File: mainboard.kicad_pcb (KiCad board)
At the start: 2 copper layers, 70 x 60 mm, 25 parts, among them J1 terminal_led-strip, J2 header_rotary-encoder, J3 AudioJack2, J4 header_rpi, J5 power_input, Q1 IRF9540N, SW1 power_switch, U1 ATtiny84A-P, U2 MSGEQ7, U3 OPA197xDBV, U4 logic-level-converter

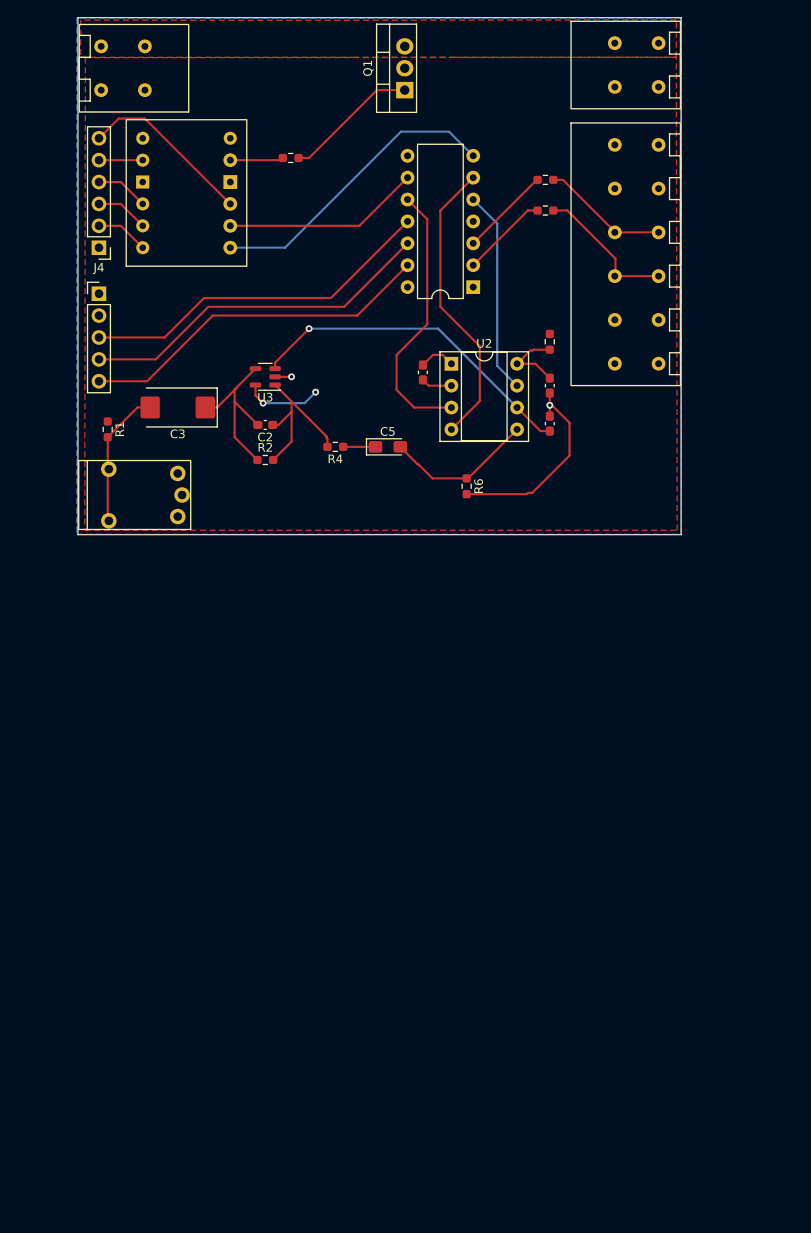
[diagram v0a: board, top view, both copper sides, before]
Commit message: start routing tracks
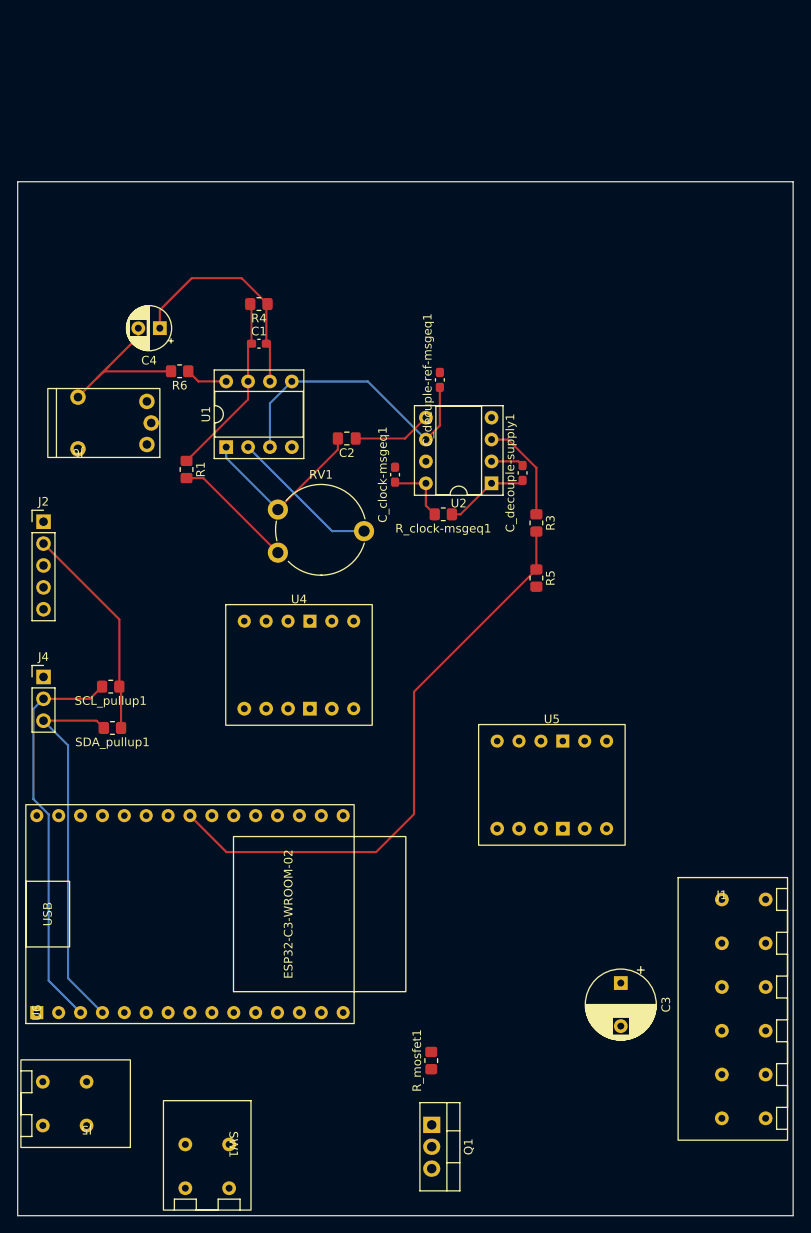
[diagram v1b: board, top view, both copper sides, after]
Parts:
- removed C5: 0.22u, Capacitor_Tantalum_SMD:CP_EIA-3216-18_Kemet-A_Pad1.58x1.35mm_HandSolder
- removed J3: AudioJack2, my_lib:jack_3.5mm_TS-only
- removed R2: 170k, Resistor_SMD:R_0603_1608Metric_Pad0.98x0.95mm_HandSolder
- removed R_led-strip_1, R_led-strip_2: 220, Resistor_SMD:R_0603_1608Metric_Pad0.98x0.95mm_HandSolder
- removed U3: OPA197xDBV, Package_TO_SOT_SMD:SOT-23-5
- added C1: 7p, Capacitor_SMD:C_0603_1608Metric_Pad1.08x0.95mm_HandSolder, F.Cu at (78.0, 68.8)
- added C4: 5.6u, Capacitor_THT:CP_Radial_D5.0mm_P2.50mm, F.Cu at (66.5, 67.0)
- added J6: AudioJack2, my_lib:jack_3.5mm_TS-only, F.Cu at (57.0, 81.0)
- added R3: 1M, Resistor_SMD:R_0805_2012Metric_Pad1.20x1.40mm_HandSolder, F.Cu at (110.2, 89.6)
- added R5: 2M, Resistor_SMD:R_0805_2012Metric_Pad1.20x1.40mm_HandSolder, F.Cu at (110.2, 96.0)
- added RV1: 5k, Potentiometer_THT:Potentiometer_Piher_PT-10-V10_Vertical, F.Cu at (80.2, 93.0)
- added SCL_pullup1: 2k, Resistor_SMD:R_0805_2012Metric_Pad1.20x1.40mm_HandSolder, F.Cu at (60.8, 108.6)
- added SDA_pullup1: 2k, Resistor_SMD:R_0805_2012Metric_Pad1.20x1.40mm_HandSolder, F.Cu at (61.0, 113.4)
- added U5: logic-level-converter, my_lib:sparkfun_logic_level_converter_bidirectional, F.Cu at (112.0, 120.0)
- added U6: ~, my_lib:esp32_c3_dev-kit-c_02, F.Cu at (52.2, 146.4)
- C2: value 7p -> C; footprint Capacitor_SMD:C_0603_1608Metric_Pad1.08x0.95mm_HandSolder -> Capacitor_SMD:C_0805_2012Metric_Pad1.18x1.45mm_HandSolder
- C3: value 5.6u -> C_Polarized; footprint Capacitor_Tantalum_SMD:CP_EIA-7343-31_Kemet-D_Pad2.25x2.55mm_HandSolder -> Capacitor_THT:CP_Radial_D8.0mm_P5.00mm
- J4: value header_rpi -> header_pi; footprint Connector_PinHeader_2.54mm:PinHeader_1x06_P2.54mm_Vertical -> Connector_PinHeader_2.54mm:PinHeader_1x03_P2.54mm_Vertical
- R1: value 6k -> 1k; footprint Resistor_SMD:R_0603_1608Metric_Pad0.98x0.95mm_HandSolder -> Resistor_SMD:R_0805_2012Metric_Pad1.20x1.40mm_HandSolder
- R4: value 50 -> 170k; footprint Resistor_SMD:R_0603_1608Metric_Pad0.98x0.95mm_HandSolder -> Resistor_SMD:R_0805_2012Metric_Pad1.20x1.40mm_HandSolder
- R6: value 100k -> 6k; footprint Resistor_SMD:R_0603_1608Metric_Pad0.98x0.95mm_HandSolder -> Resistor_SMD:R_0805_2012Metric_Pad1.20x1.40mm_HandSolder
- R_clock-msgeq1, R_mosfet1: footprint Resistor_SMD:R_0603_1608Metric_Pad0.98x0.95mm_HandSolder -> Resistor_SMD:R_0805_2012Metric_Pad1.20x1.40mm_HandSolder
- U1: value ATtiny84A-P -> OPA2277; footprint Package_DIP:DIP-14_W7.62mm -> Package_DIP:DIP-8_W7.62mm_Socket
- moved SW1 135.4 mm to (74.5, 161.7), turned to -90 degrees
- moved J5 120.4 mm to (58.0, 159.5)
- moved Q1 120.1 mm to (98.1, 159.5), turned to -90 degrees
- moved R_mosfet1 106.0 mm to (98.0, 152.0), turned to 90 degrees
- moved J1 88.5 mm to (131.7, 133.3)
- moved C3 84.3 mm to (120.0, 143.0), turned to -90 degrees
- moved U4 56.3 mm to (82.7, 106.1), turned to 0 degrees
- moved J4 50.2 mm to (53.0, 107.5), turned to 0 degrees
- moved R6 35.9 mm to (68.8, 72.0), turned to 180 degrees
- moved U1 34.2 mm to (74.2, 80.8), turned to 90 degrees
- moved J2 27.2 mm to (53.0, 89.5)
- moved R_clock-msgeq1 23.5 mm to (99.4, 88.6), turned to 180 degrees
- moved C_clock-msgeq1 20.7 mm to (93.8, 84.0), turned to 90 degrees
- moved R4 18.8 mm to (78.0, 64.2)
- moved C_decouple-supply1 16.4 mm to (108.6, 83.8), turned to 90 degrees
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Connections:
- C2 pad 1: Net-(C2-Pad1) -> msgeq7-in
- C2 pad 2: Net-(U3--) -> Net-(C2-Pad2)
- C3 pad 1: Net-(U3--) -> 5V_led
- C3 pad 2: Net-(C3-Pad2) -> GND
- C_decouple-supply1 pad 1: /power-on -> 5V
- C_decuple-ref-msgeq1 pad 1: Net-(U2-GND) -> V_ref
- J1 pad 1: /power-on -> GND
- J1 pad 2: /power-on -> Net-(J1-Pin_2)
- J1 pad 3: Net-(J1-Pin_3) -> 5V_led
- J1 pad 4: Net-(J1-Pin_4) -> GND
- J1 pad 5: GND -> Net-(J1-Pin_5)
- J1 pad 6: GND -> 5V_led
- J2 pad 2: /power-on -> 3V3
- J2 pad 3: Net-(J2-Pin_3) -> rotary_sw
- J2 pad 4: Net-(J2-Pin_4) -> rotary_dt
- J2 pad 5: Net-(J2-Pin_5) -> rotary_clk
- Q1 pad 2: /power-on -> 5V_led
- Q1 pad 3: +5V -> 5V
- R1 pad 1: /power-on -> preamp_out
- R1 pad 2: Net-(C3-Pad2) -> Net-(R1-Pad2)
- R4 pad 1: Net-(C5-Pad1) -> Net-(U1B--)
- R4 pad 2: Net-(C2-Pad1) -> preamp_out
- R6 pad 1: Net-(U2-IN) -> 5V
- R6 pad 2: GND -> Net-(C4-Pad2)
- R_clock-msgeq1 pad 1: /power-on -> 5V
- R_mosfet1 pad 1: Net-(U4-LV3) -> power_fet
- SW1 pad 1: +5V -> 5V
- SW1 pad 2: /power-on -> +5V
- U1 pad 1: /power-on -> Net-(C2-Pad2)
- U1 pad 3: Net-(U1-XTAL2/PB1) -> V_ref
- U1 pad 4: unconnected-(U1-~{RESET}/PB3-Pad4) -> GND
- U1 pad 5: Net-(U1-PB2) -> V_ref
- U1 pad 6: Net-(U1-PA7) -> Net-(U1B--)
- U1 pad 7: Net-(U1-PA6) -> preamp_out
- U1 pad 8: unconnected-(U1-PA5-Pad8) -> 5V
- U2 pad 1: /power-on -> 5V
- U2 pad 3: Net-(U1-PA3) -> msgeq7-out
- U2 pad 4: Net-(U1-PA7) -> msgeq7-strobe
- U2 pad 5: Net-(U2-IN) -> msgeq7-in
- U2 pad 6: Net-(U2-GND) -> V_ref
- U2 pad 7: Net-(U1-PB2) -> msgeq7-reset
- U4 pad 1: Net-(U1-PA6) -> esp_led-strip_front
- U4 pad 10: Net-(J4-Pin_4) -> 5V
- U4 pad 11: Net-(J4-Pin_3) -> Net-(J1-Pin_5)
- U4 pad 12: Net-(J4-Pin_2) -> Net-(J1-Pin_2)
- U4 pad 2: Net-(U1-PA4) -> esp_led-strip_back
- U4 pad 3: Net-(J4-Pin_6) -> 3V3
- U4 pad 5: Net-(U4-LV3) -> esp_msgeq7-strobe
- U4 pad 6: unconnected-(U4-LV4-Pad6) -> esp_msgeq7-reset
- U4 pad 7: unconnected-(U4-HV4-Pad7) -> msgeq7-reset
- U4 pad 8: Net-(J4-Pin_5) -> msgeq7-strobe
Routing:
- net Net-(U6-4): track 0.00 -> 68.3 mm
- net Net-(J2-Pin_5): track 41.4 -> 0.00 mm
- net Net-(J2-Pin_4): track 41.4 -> 0.00 mm
- net Net-(J2-Pin_3): track 41.4 -> 0.00 mm
- net Net-(J4-Pin_2): track 6.13 -> 46.6 mm
- net Net-(U2-GND): track 39.1 -> 0.00 mm, vias 1 -> 0
- net Net-(J4-Pin_3): track 6.13 -> 44.1 mm
- net Net-(U1-PA6): track 34.9 -> 0.00 mm
- net Net-(U1-PA7): track 34.1 -> 0.00 mm
- net V_ref: track 0.00 -> 33.8 mm
- net Net-(U1-PA3): track 31.7 -> 0.00 mm
- net Net-(U1B--): track 0.00 -> 26.6 mm
- net 3V3: track 0.00 -> 25.1 mm
- net GND: track 28.9 -> 3.80 mm, vias 2 -> 0
- net Net-(U1-PB2): track 23.7 -> 0.00 mm
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- removed copper zone on F.Cu, net +5V
- removed copper zone on F.Cu, net /power-on
- removed copper zone on B.Cu, net GND
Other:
- board size 70 x 60 mm -> 90 x 120 mm

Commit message: route tracks and add mounting holes
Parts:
- removed U6: ~, my_lib:esp32_c3_dev-kit-c_02
- added REF**: MountingHole_3.2mm_M3_DIN965_Pad, MountingHole:MountingHole_3.2mm_M3_DIN965_Pad, F.Cu at (125.0, 65.0)
- added REF**: MountingHole_3.2mm_M3_DIN965_Pad, MountingHole:MountingHole_3.2mm_M3_DIN965_Pad, F.Cu at (55.0, 165.0)
- added REF**: MountingHole_3.2mm_M3_DIN965_Pad, MountingHole:MountingHole_3.2mm_M3_DIN965_Pad, F.Cu at (125.0, 165.0)
- added REF**: MountingHole_3.2mm_M3_DIN965_Pad, MountingHole:MountingHole_3.2mm_M3_DIN965_Pad, F.Cu at (55.0, 65.0)
- added U3: ~, my_lib:esp32_c3_dev-kit-c_02, F.Cu at (52.2, 146.4)
- C1, C_clock-msgeq1, C_decouple-supply1, C_decuple-ref-msgeq1: footprint Capacitor_SMD:C_0603_1608Metric_Pad1.08x0.95mm_HandSolder -> Capacitor_SMD:C_0805_2012Metric_Pad1.18x1.45mm_HandSolder
- moved C3 16.0 mm to (108.4, 154.0)
- moved J1 10.2 mm to (121.5, 133.2)
- moved J5 2.54 mm to (58.0, 157.0)
- turned R_mosfet1 to -90 degrees
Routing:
- net 5V: track 15.0 -> 172.8 mm
- net rotary_sw: track 0.00 -> 89.4 mm, vias 0 -> 1
- net Net-(J1-Pin_5): track 0.00 -> 88.7 mm
- net rotary_dt: track 0.00 -> 87.9 mm, vias 0 -> 1
- net rotary_clk: track 0.00 -> 86.4 mm, vias 0 -> 1
- net 3V3: track 25.1 -> 102.1 mm
- net Net-(J1-Pin_2): track 0.00 -> 70.1 mm
- net Net-(U3-GPIO10): track 0.00 -> 49.7 mm
- net power_fet: track 0.00 -> 44.4 mm
- net msgeq7-strobe: track 0.00 -> 35.5 mm
- net esp_msgeq7-reset: track 0.00 -> 28.0 mm
- net esp_led-strip_back: track 0.00 -> 25.6 mm
- net msgeq7-reset: track 0.00 -> 22.0 mm
- net Net-(U3-GPIO4/ADC1_CH4): track 68.3 -> 51.4 mm
- net esp_led-strip_front: track 0.00 -> 16.1 mm
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- added copper zone on F.Cu, net +5V
- added copper zone on F.Cu, net 5V
- added copper zone on F.Cu, net 5V_led
- added copper zone on B.Cu, net GND
- added copper zone on F.Cu, net GND
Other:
- board size 90 x 120 mm -> 80 x 110 mm

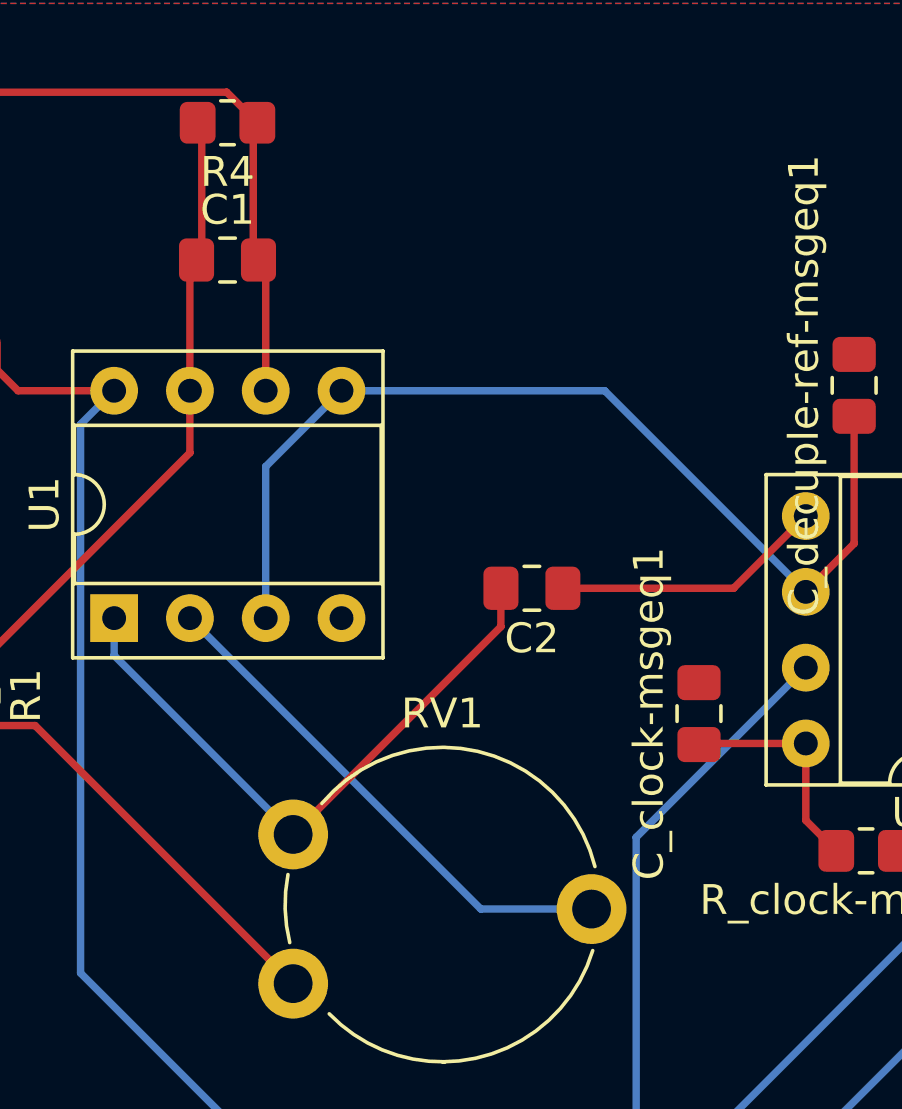
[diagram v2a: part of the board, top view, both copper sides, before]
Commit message: add jlc part ids
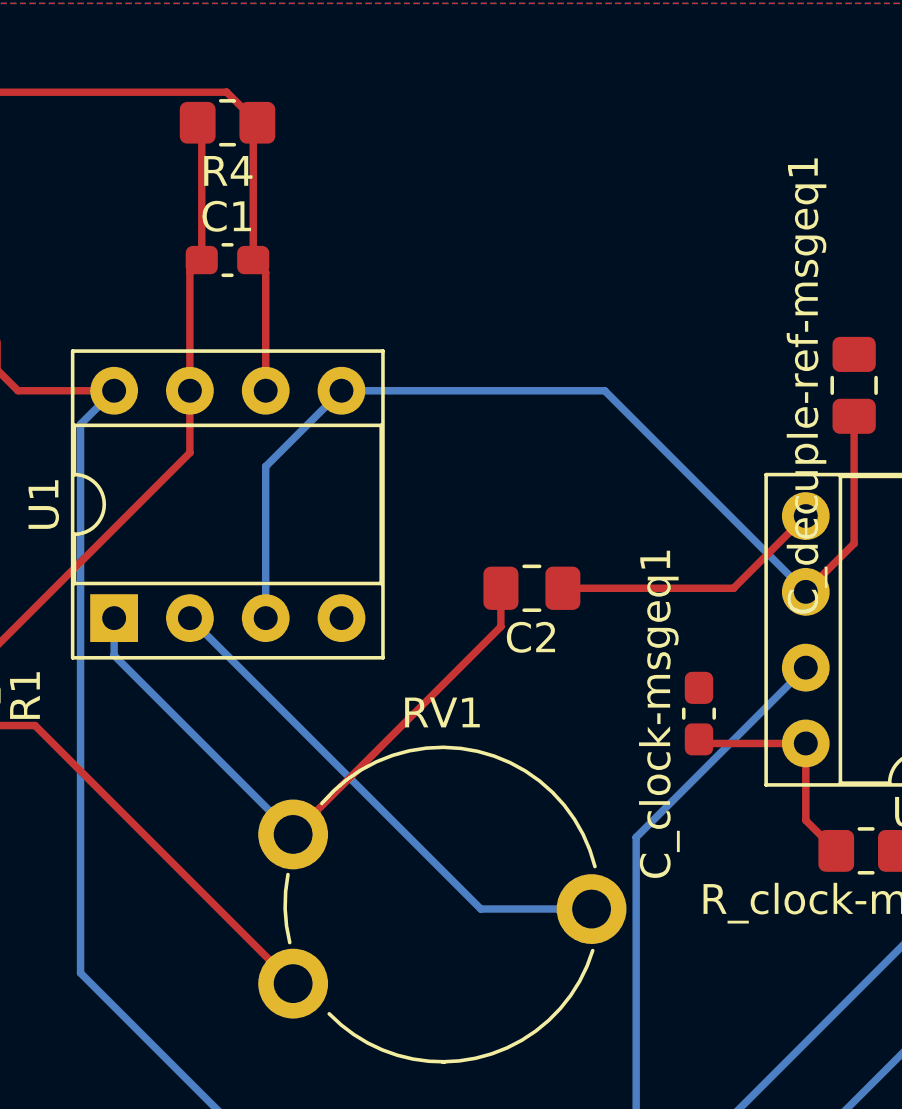
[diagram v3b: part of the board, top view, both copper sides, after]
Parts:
- C1: value 7p -> 10p; footprint Capacitor_SMD:C_0805_2012Metric_Pad1.18x1.45mm_HandSolder -> Capacitor_SMD:C_0603_1608Metric_Pad1.08x0.95mm_HandSolder
- C2: value C -> 220n
- C_clock-msgeq1: footprint Capacitor_SMD:C_0805_2012Metric_Pad1.18x1.45mm_HandSolder -> Capacitor_SMD:C_0603_1608Metric_Pad1.08x0.95mm_HandSolder
- R4: value 170k -> 150k
- R6: value 6k -> 5k6

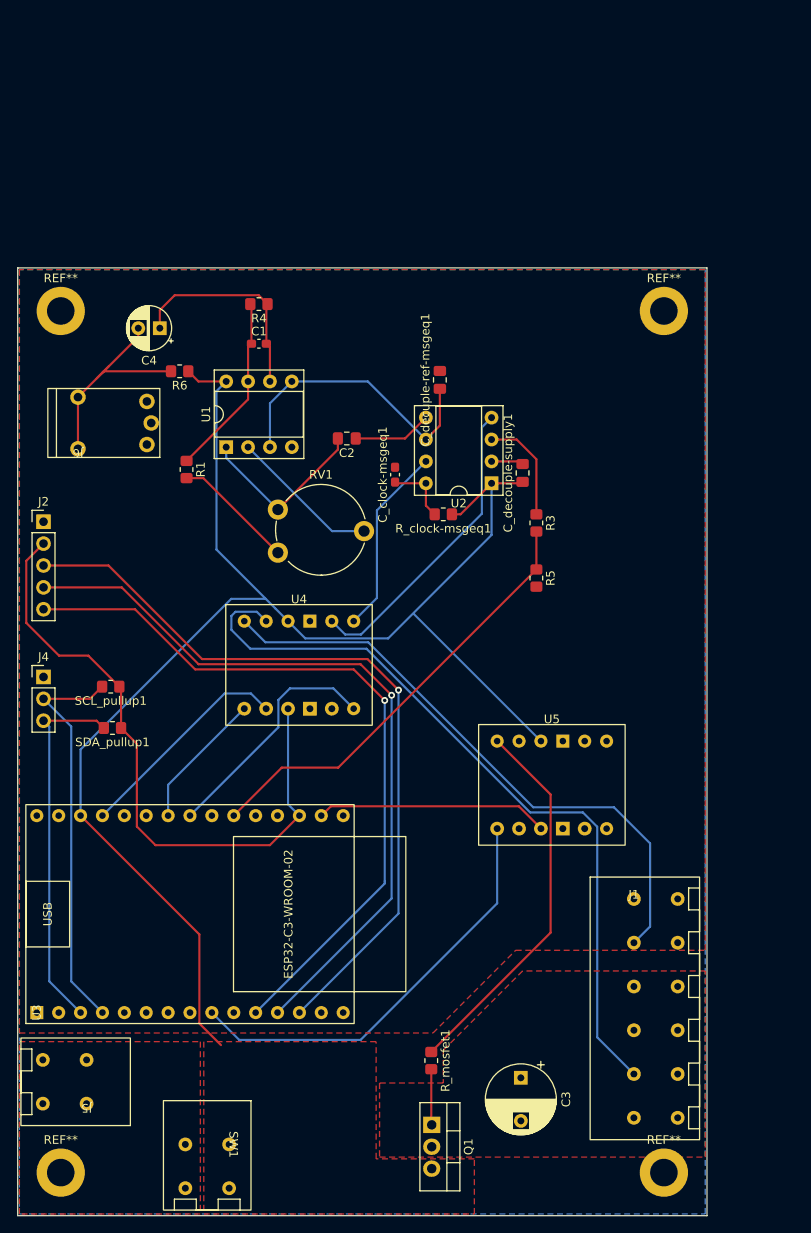
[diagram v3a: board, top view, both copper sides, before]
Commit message: flip rotary encoder connector
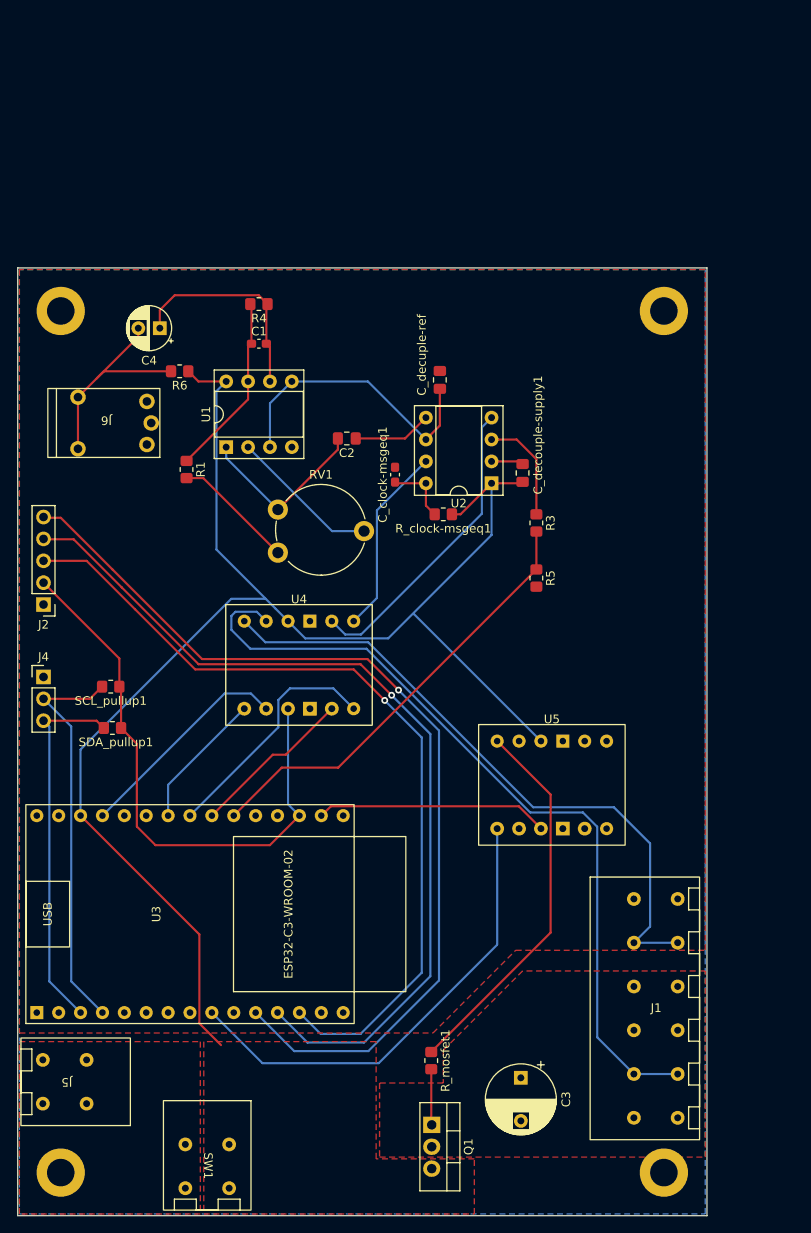
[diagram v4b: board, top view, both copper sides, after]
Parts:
- moved J2 9.62 mm to (53.0, 99.1), turned to 180 degrees
- renumbered C_decuple-ref-msgeq1 to C_decuple-ref
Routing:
- net rotary_clk: track 86.4 -> 111.7 mm
- net esp_msgeq7-strobe: track 0.00 -> 19.1 mm
- net rotary_dt: track 87.9 -> 104.7 mm
- net rotary_sw: track 89.4 -> 97.8 mm
- net 3V3: track 102.1 -> 93.9 mm
- net Net-(J1-Pin_5): track 88.7 -> 93.8 mm
- net Net-(J1-Pin_2): track 70.1 -> 75.2 mm
- net Net-(U3-GPIO10): track 49.7 -> 54.7 mm
- net Net-(C4-Pad2): track 27.0 -> 25.8 mm
